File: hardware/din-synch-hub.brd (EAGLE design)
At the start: 140.7 x 20.2 mm, 47 parts, among them IC1 4050D, IC2 REG1117, IC3 4050D, IC4 PIC12F1822SO08, IC5 6N138, X1 DIN5PIN, X2 DIN5PIN, X3 DIN5PIN, X4 DIN5PIN, X5 DIN5PIN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

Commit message: fix bug
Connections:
- net N$4: now also X1.4; no longer X1.1
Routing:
- net N$4: track 10.3 -> 6.69 mm, vias 1 -> 0
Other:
- board text added: "six4pix.com/synchole"
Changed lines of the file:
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@@
 <text x="111.887" y="17.399" size="1.778" layer="21" font="vector">hotchk155</text>
 <text x="32.54375" y="15.24" size="3.81" layer="21" font="vector">Sync Hole</text>
+<text x="32.41675" y="7.4295" size="1.778" layer="21" font="vector">six4pix.com/synchole</text>
 </plain>
 <attributes>
@@
 </signal>
 <signal name="N$4">
-<contactref element="X1" pad="1"/>
 <contactref element="R18" pad="1"/>
-<wire x1="22.44725" y1="7.33675" x2="22.44725" y2="2.4765" width="0.3048" layer="16"/>
-<via x="23.495" y="1.42875" extent="1-16" drill="0.6"/>
-<wire x1="23.495" y1="3.302" x2="23.495" y2="4.445" width="0.3048" layer="1"/>
-<wire x1="23.495" y1="4.445" x2="22.86" y2="5.08" width="0.3048" layer="1"/>
-<wire x1="22.44725" y1="2.4765" x2="23.495" y2="1.42875" width="0.3048" layer="16"/>
-<wire x1="23.495" y1="1.42875" x2="23.495" y2="3.302" width="0.3048" layer="1"/>
+<contactref element="X1" pad="4"/>
+<wire x1="26.035" y1="3.302" x2="24.03475" y2="3.302" width="0.4064" layer="16"/>
+<wire x1="24.03475" y1="3.302" x2="22.44725" y2="4.8895" width="0.4064" layer="16"/>
+<wire x1="22.44725" y1="4.8895" x2="22.44725" y2="7.33675" width="0.4064" layer="16"/>
 </signal>
 <signal name="N$3">

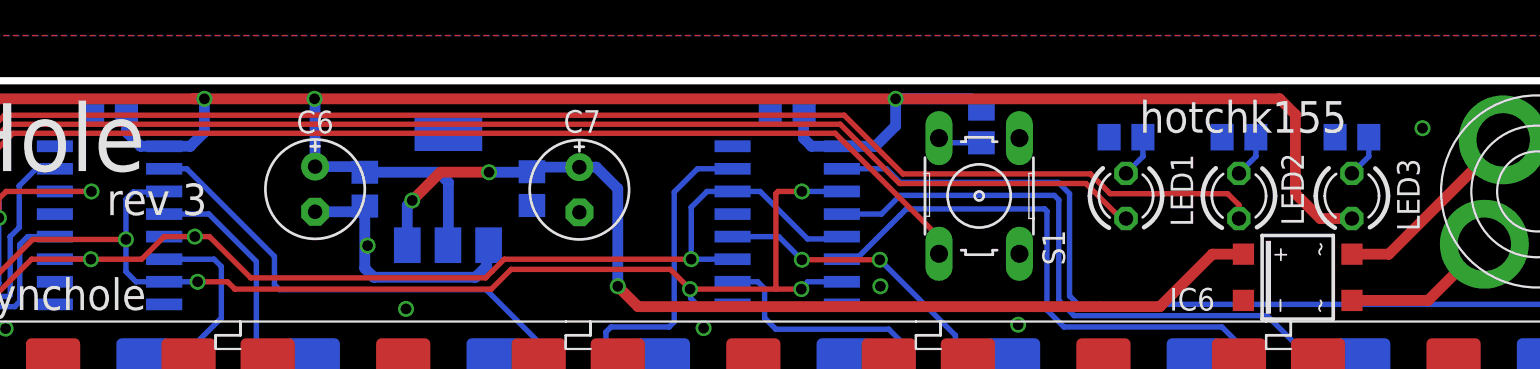
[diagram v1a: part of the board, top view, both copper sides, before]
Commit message: REV4
moved leds to match bsplit
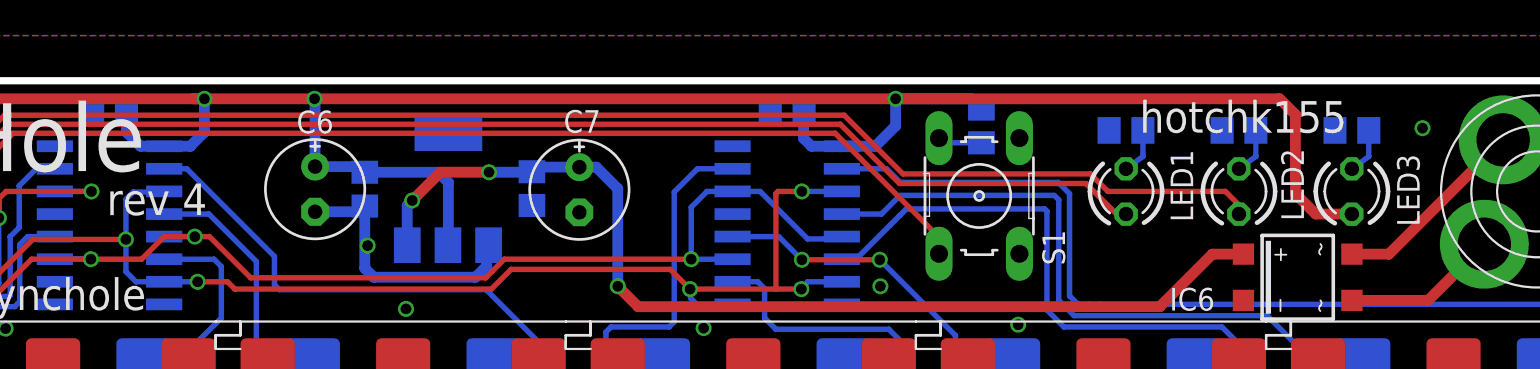
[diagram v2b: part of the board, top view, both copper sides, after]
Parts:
- moved R1 0.38 mm to (123.8, 17.5)
- moved R2 0.38 mm to (117.5, 17.5)
- moved R3 0.38 mm to (111.1, 17.5)
- moved LED1 0.25 mm to (111.1, 14.1)
- moved LED2 0.25 mm to (117.5, 14.1)
- moved LED3 0.25 mm to (123.8, 14.1)
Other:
- board text added: "rev 4"
- board text removed: "rev 3"
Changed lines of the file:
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@@
 <wire x1="139.192" y1="20.32" x2="140.843" y2="18.796" width="0.4064" layer="20" curve="-90"/>
 <wire x1="140.843" y1="18.796" x2="140.843" y2="1.27" width="0.4064" layer="20"/>
-<text x="53.81625" y="12.7635" size="1.778" layer="21" font="vector">rev 3</text>
+<text x="53.81625" y="12.7635" size="1.778" layer="21" font="vector">rev 4</text>
 <text x="111.887" y="17.399" size="1.778" layer="21" font="vector">hotchk155</text>
 <text x="32.54375" y="15.24" size="3.81" layer="21" font="vector">Sync Hole</text>
@@
 </class>
 </classes>
-<designrules name="ITEADstudio_DRC">
-<description language="de">&lt;b&gt;EAGLE Design Rules&lt;/b&gt;
+<designrules name="hackvana">
+<description language="de">&lt;b&gt;EAGLE Design Rules für Hackvana&lt;/b&gt;
 &lt;p&gt;
 Die Standard-Design-Rules sind so gewählt, dass sie für
@@
 Einstellungen hier und speichern die Design Rules unter
 einem neuen Namen ab.</description>
-<description language="en">&lt;b&gt;EAGLE Design Rules&lt;/b&gt;
+<description language="en">&lt;b&gt;EAGLE Design Rules for Hackvana&lt;/b&gt;
 &lt;p&gt;
 The default Design Rules have been set to cover
@@
 necessary adjustments and save your customized
 design rules under a new name.</description>
-<description language="zh">&lt;b&gt;Seeed Studio EAGLE Design Rules&lt;/b&gt;
+<description language="zh">&lt;b&gt;EAGLE Design Rules for Hackvana&lt;/b&gt;
 </description>
 <param name="layerSetup" value="(1*16)"/>
@@
 <param name="mtIsolate" value="1.5mm 0.15mm 0.2mm 0.15mm 0.2mm 0.15mm 0.2mm 0.15mm 0.2mm 0.15mm 0.2mm 0.15mm 0.2mm 0.15mm 0.2mm"/>
 <param name="mdWireWire" value="6mil"/>
-<param name="mdWirePad" value="6mil"/>
+<param name="mdWirePad" value="9mil"/>
 <param name="mdWireVia" value="6mil"/>
 <param name="mdPadPad" value="6mil"/>
@@
 <param name="mdViaViaSameLayer" value="8mil"/>
 <param name="mnLayersViaInSmd" value="2"/>
-<param name="mdCopperDimension" value="10mil"/>
-<param name="mdDrill" value="10mil"/>
+<param name="mdCopperDimension" value="6mil"/>
+<param name="mdDrill" value="6mil"/>
 <param name="mdSmdStop" value="0mil"/>
 <param name="msWidth" value="6mil"/>
-<param name="msDrill" value="12mil"/>
-<param name="msMicroVia" value="12mil"/>
+<param name="msDrill" value="0.3mm"/>
+<param name="msMicroVia" value="0.25mm"/>
 <param name="msBlindViaRatio" value="0.5"/>
 <param name="rvPadTop" value="0.25"/>
@@
 <attribute name="VALUE" x="97.79" y="16.891" size="1.27" layer="27" ratio="10" rot="R270"/>
 </element>
-<element name="LED1" library="led" package="LED3MM" value="" x="111.125" y="13.843" smashed="yes" rot="R90">
-<attribute name="NAME" x="113.63325" y="16.1925" size="1.27" layer="25" ratio="10" rot="R270"/>
-<attribute name="VALUE" x="112.776" y="15.748" size="1.27" layer="27" ratio="10" rot="R90"/>
-</element>
-<element name="R3" library="rcl" package="R0805" value="" x="111.125" y="17.145" smashed="yes" rot="MR180">
-<attribute name="NAME" x="109.7915" y="19.71675" size="1.27" layer="26" rot="MR180"/>
-<attribute name="VALUE" x="110.49" y="19.685" size="1.27" layer="28" rot="MR180"/>
-</element>
-<element name="LED2" library="led" package="LED3MM" value="" x="117.475" y="13.843" smashed="yes" rot="R90">
-<attribute name="NAME" x="119.85625" y="16.256" size="1.27" layer="25" ratio="10" rot="R270"/>
-<attribute name="VALUE" x="119.126" y="15.748" size="1.27" layer="27" ratio="10" rot="R90"/>
-</element>
-<element name="R2" library="rcl" package="R0805" value="" x="117.475" y="17.145" smashed="yes" rot="MR180">
-<attribute name="NAME" x="116.459" y="19.685" size="1.27" layer="26" rot="MR180"/>
-<attribute name="VALUE" x="116.84" y="19.685" size="1.27" layer="28" rot="MR180"/>
+<element name="LED1" library="led" package="LED3MM" value="" x="111.125" y="14.097" smashed="yes" rot="R90">
+<attribute name="NAME" x="113.63325" y="16.4465" size="1.27" layer="25" ratio="10" rot="R270"/>
+<attribute name="VALUE" x="112.776" y="16.002" size="1.27" layer="27" ratio="10" rot="R90"/>
+</element>
+<element name="R3" library="rcl" package="R0805" value="" x="111.125" y="17.526" smashed="yes" rot="MR180">
+<attribute name="NAME" x="109.9185" y="19.8755" size="1.27" layer="26" rot="MR180"/>
+<attribute name="VALUE" x="110.49" y="20.066" size="1.27" layer="28" rot="MR180"/>
+</element>
+<element name="LED2" library="led" package="LED3MM" value="" x="117.475" y="14.097" smashed="yes" rot="R90">
+<attribute name="NAME" x="119.85625" y="16.51" size="1.27" layer="25" ratio="10" rot="R270"/>
+<attribute name="VALUE" x="119.126" y="16.002" size="1.27" layer="27" ratio="10" rot="R90"/>
+</element>
+<element name="R2" library="rcl" package="R0805" value="" x="117.475" y="17.526" smashed="yes" rot="MR180">
+<attribute name="NAME" x="116.332" y="19.8755" size="1.27" layer="26" rot="MR180"/>
+<attribute name="VALUE" x="116.84" y="20.066" size="1.27" layer="28" rot="MR180"/>
 </element>
 <element name="IC2" library="burr-brown" package="SOT223" value="REG1117" x="73.025" y="14.224" smashed="yes" rot="MR0">
@@
 <attribute name="VALUE" x="62.992" y="11.557" size="1.27" layer="27" ratio="10" rot="R270"/>
 </element>
-<element name="R1" library="rcl" package="R0805" value="" x="123.825" y="17.145" smashed="yes" rot="MR180">
-<attribute name="NAME" x="123.09475" y="19.6215" size="1.27" layer="26" rot="MR180"/>
-<attribute name="VALUE" x="123.19" y="19.685" size="1.27" layer="28" rot="MR180"/>
-</element>
-<element name="LED3" library="led" package="LED3MM" value="" x="123.825" y="13.843" smashed="yes" rot="R90">
-<attribute name="NAME" x="126.365" y="15.9385" size="1.27" layer="25" ratio="10" rot="R270"/>
-<attribute name="VALUE" x="125.476" y="15.748" size="1.27" layer="27" ratio="10" rot="R90"/>
+<element name="R1" library="rcl" package="R0805" value="" x="123.825" y="17.526" smashed="yes" rot="MR180">
+<attribute name="NAME" x="122.4915" y="19.84375" size="1.27" layer="26" rot="MR180"/>
+<attribute name="VALUE" x="123.19" y="20.066" size="1.27" layer="28" rot="MR180"/>
+</element>
+<element name="LED3" library="led" package="LED3MM" value="" x="123.825" y="14.097" smashed="yes" rot="R90">
+<attribute name="NAME" x="126.365" y="16.1925" size="1.27" layer="25" ratio="10" rot="R270"/>
+<attribute name="VALUE" x="125.476" y="16.002" size="1.27" layer="27" ratio="10" rot="R90"/>
 </element>
 <element name="U$1" library="jason_eagle6" package="PWR_SOCKET_2_1MM" value="PWR_SOCKET_2_1MM" x="134.239" y="14.097" smashed="yes" rot="R135"/>
@@
 <wire x1="119.761" y1="19.304" x2="120.65" y2="18.415" width="0.6096" layer="1"/>
 <wire x1="120.65" y1="18.415" x2="120.65" y2="13.97" width="0.6096" layer="1"/>
-<wire x1="120.65" y1="13.97" x2="122.047" y2="12.573" width="0.6096" layer="1"/>
-<wire x1="122.047" y1="12.573" x2="123.825" y2="12.573" width="0.6096" layer="1"/>
+<wire x1="120.65" y1="13.97" x2="121.793" y2="12.827" width="0.6096" layer="1"/>
+<wire x1="121.793" y1="12.827" x2="123.825" y2="12.827" width="0.6096" layer="1"/>
 </signal>
 <signal name="N$14">
@@
 <contactref element="IC4" pad="3"/>
 <contactref element="LED1" pad="A"/>
-<wire x1="111.125" y1="12.573" x2="110.83925" y2="12.573" width="0.3048" layer="1"/>
+<wire x1="111.125" y1="12.827" x2="110.83925" y2="12.573" width="0.3048" layer="1"/>
 <wire x1="110.83925" y1="12.573" x2="108.87075" y2="14.5415" width="0.3048" layer="1"/>
 <wire x1="108.87075" y1="14.5415" x2="98.39325" y2="14.5415" width="0.3048" layer="1"/>
@@
 <contactref element="IC4" pad="5"/>
 <contactref element="LED2" pad="A"/>
-<wire x1="117.475" y1="12.573" x2="117.475" y2="13.335" width="0.3048" layer="1"/>
-<wire x1="117.475" y1="13.335" x2="116.84" y2="13.97" width="0.3048" layer="1"/>
-<wire x1="116.84" y1="13.97" x2="110.236" y2="13.97" width="0.3048" layer="1"/>
-<wire x1="110.236" y1="13.97" x2="109.12475" y2="15.08125" width="0.3048" layer="1"/>
+<wire x1="117.475" y1="12.827" x2="117.475" y2="13.335" width="0.3048" layer="1"/>
+<wire x1="117.475" y1="13.335" x2="116.713" y2="14.097" width="0.3048" layer="1"/>
+<wire x1="116.713" y1="14.097" x2="110.109" y2="14.097" width="0.3048" layer="1"/>
+<wire x1="110.109" y1="14.097" x2="109.12475" y2="15.08125" width="0.3048" layer="1"/>
 <wire x1="109.12475" y1="15.08125" x2="98.58375" y2="15.08125" width="0.3048" layer="1"/>
 <wire x1="38.5318" y1="11.303" x2="38.5318" y2="10.1727" width="0.3048" layer="16"/>
@@
 <contactref element="R1" pad="2"/>
 <contactref element="LED3" pad="K"/>
-<wire x1="124.775" y1="17.145" x2="124.775" y2="16.063" width="0.3048" layer="16"/>
-<wire x1="124.775" y1="16.063" x2="123.825" y2="15.113" width="0.3048" layer="16"/>
+<wire x1="124.775" y1="17.526" x2="124.775" y2="16.063" width="0.3048" layer="16"/>
+<wire x1="124.775" y1="16.063" x2="123.825" y2="15.367" width="0.3048" layer="16"/>
 </signal>
 <signal name="N$31">
 <contactref element="R2" pad="2"/>
 <contactref element="LED2" pad="K"/>
-<wire x1="118.425" y1="17.145" x2="118.425" y2="16.063" width="0.3048" layer="16"/>
-<wire x1="118.425" y1="16.063" x2="117.475" y2="15.113" width="0.3048" layer="16"/>
+<wire x1="118.425" y1="17.526" x2="118.425" y2="16.063" width="0.3048" layer="16"/>
+<wire x1="118.425" y1="16.063" x2="117.475" y2="15.367" width="0.3048" layer="16"/>
 </signal>
 <signal name="N$33">
 <contactref element="R3" pad="2"/>
 <contactref element="LED1" pad="K"/>
-<wire x1="112.075" y1="17.145" x2="112.075" y2="16.063" width="0.3048" layer="16"/>
-<wire x1="112.075" y1="16.063" x2="111.125" y2="15.113" width="0.3048" layer="16"/>
+<wire x1="112.075" y1="17.526" x2="112.075" y2="16.063" width="0.3048" layer="16"/>
+<wire x1="112.075" y1="16.063" x2="111.125" y2="15.367" width="0.3048" layer="16"/>
 </signal>
 <signal name="MIDI">

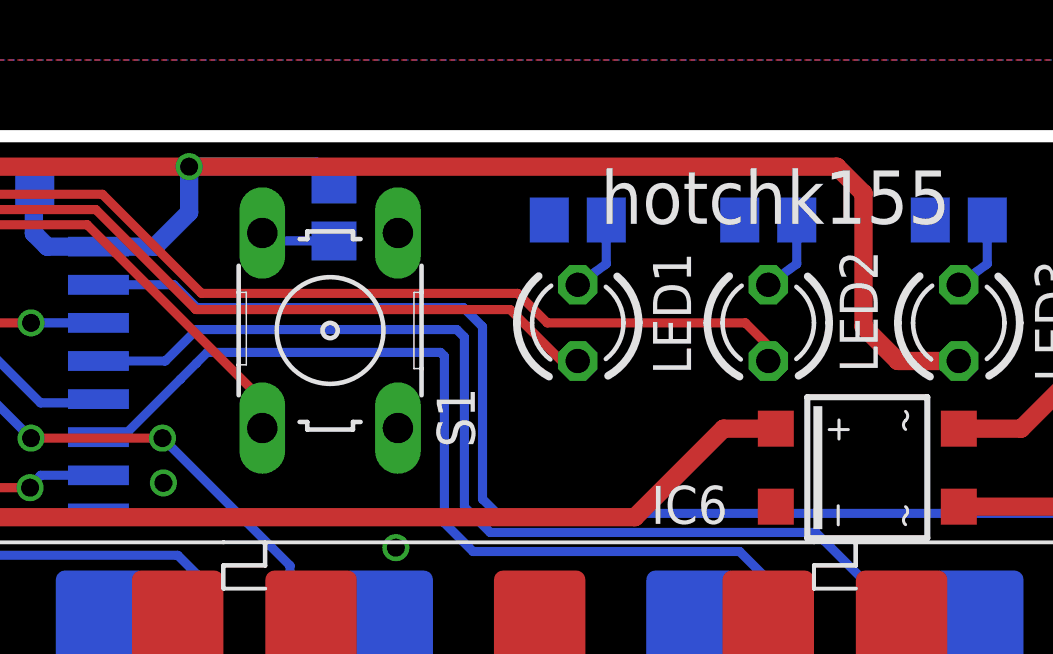
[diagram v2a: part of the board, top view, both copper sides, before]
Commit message: move switch (rev4 pcb)
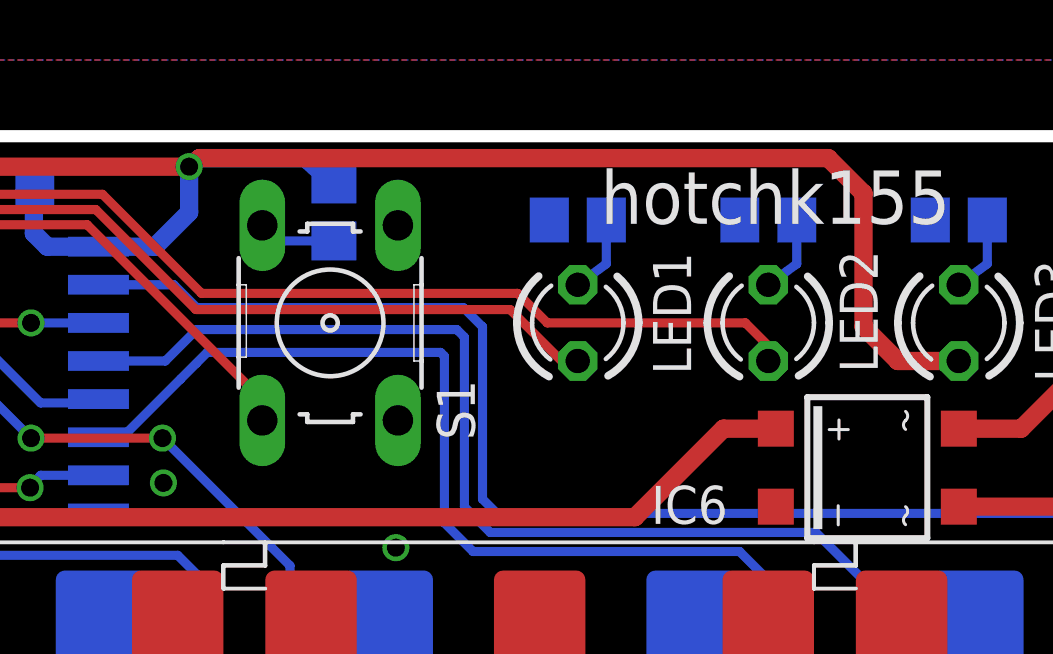
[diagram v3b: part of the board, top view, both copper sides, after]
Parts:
- moved S1 0.25 mm to (102.9, 14.1)
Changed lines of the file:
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@@
 <attribute name="VALUE" x="100.457" y="17.145" size="1.27" layer="28" rot="MR90"/>
 </element>
-<element name="S1" library="switch-omron" package="B3F-10XX" value="" x="102.87" y="13.843" smashed="yes" rot="R270">
-<attribute name="OC_NEWARK" value="36M3542" x="53.34" y="-48.387" size="1.778" layer="27" rot="R270" display="off"/>
-<attribute name="MPN" value="B3F-1000" x="53.34" y="-48.387" size="1.778" layer="27" rot="R270" display="off"/>
-<attribute name="MF" value="" x="53.34" y="-48.387" size="1.778" layer="27" rot="R270" display="off"/>
-<attribute name="OC_FARNELL" value="176432" x="53.34" y="-48.387" size="1.778" layer="27" rot="R270" display="off"/>
-<attribute name="NAME" x="106.426" y="11.938" size="1.27" layer="25" ratio="10" rot="R270"/>
-<attribute name="VALUE" x="97.79" y="16.891" size="1.27" layer="27" ratio="10" rot="R270"/>
+<element name="S1" library="switch-omron" package="B3F-10XX" value="" x="102.87" y="14.097" smashed="yes" rot="R270">
+<attribute name="OC_NEWARK" value="36M3542" x="53.34" y="-48.133" size="1.778" layer="27" rot="R270" display="off"/>
+<attribute name="MPN" value="B3F-1000" x="53.34" y="-48.133" size="1.778" layer="27" rot="R270" display="off"/>
+<attribute name="MF" value="" x="53.34" y="-48.133" size="1.778" layer="27" rot="R270" display="off"/>
+<attribute name="OC_FARNELL" value="176432" x="53.34" y="-48.133" size="1.778" layer="27" rot="R270" display="off"/>
+<attribute name="NAME" x="106.426" y="12.192" size="1.27" layer="25" ratio="10" rot="R270"/>
+<attribute name="VALUE" x="97.79" y="17.145" size="1.27" layer="27" ratio="10" rot="R270"/>
 </element>
 <element name="LED1" library="led" package="LED3MM" value="" x="111.125" y="14.097" smashed="yes" rot="R90">
@@
 <wire x1="42.51325" y1="19.304" x2="59.309" y2="19.304" width="0.6096" layer="1"/>
 <wire x1="65.50025" y1="19.304" x2="98.171" y2="19.304" width="0.6096" layer="1"/>
-<wire x1="98.171" y1="19.304" x2="102.423" y2="19.304" width="0.6096" layer="16"/>
-<wire x1="102.423" y1="19.304" x2="102.997" y2="18.73" width="0.6096" layer="16"/>
+<wire x1="102.042" y1="19.58975" x2="102.997" y2="18.73" width="0.6096" layer="16"/>
 <wire x1="43.7642" y1="15.113" x2="43.7642" y2="16.4973" width="0.6096" layer="16"/>
 <wire x1="43.7642" y1="16.4973" x2="42.9895" y2="17.272" width="0.6096" layer="16"/>
@@
 <wire x1="30.607" y1="15.14475" x2="33.24225" y2="15.14475" width="0.6096" layer="16"/>
 <wire x1="33.24225" y1="15.14475" x2="33.274" y2="15.113" width="0.6096" layer="16"/>
-<wire x1="98.171" y1="19.304" x2="119.761" y2="19.304" width="0.6096" layer="1"/>
-<wire x1="119.761" y1="19.304" x2="120.65" y2="18.415" width="0.6096" layer="1"/>
+<wire x1="119.47525" y1="19.58975" x2="120.65" y2="18.415" width="0.6096" layer="1"/>
 <wire x1="120.65" y1="18.415" x2="120.65" y2="13.97" width="0.6096" layer="1"/>
 <wire x1="120.65" y1="13.97" x2="121.793" y2="12.827" width="0.6096" layer="1"/>
 <wire x1="121.793" y1="12.827" x2="123.825" y2="12.827" width="0.6096" layer="1"/>
+<wire x1="98.171" y1="19.304" x2="98.52025" y2="19.58975" width="0.6096" layer="1"/>
+<wire x1="98.52025" y1="19.58975" x2="119.47525" y2="19.58975" width="0.6096" layer="1"/>
+<wire x1="98.171" y1="19.304" x2="98.52025" y2="19.58975" width="0.6096" layer="16"/>
+<wire x1="98.52025" y1="19.58975" x2="102.042" y2="19.58975" width="0.6096" layer="16"/>
 </signal>
 <signal name="N$14">
@@
 <contactref element="R4" pad="1"/>
 <wire x1="102.997" y1="16.83" x2="100.8736" y2="16.83" width="0.3048" layer="16"/>
-<wire x1="100.8736" y1="16.83" x2="100.6094" y2="17.0942" width="0.3048" layer="16"/>
-<wire x1="100.6094" y1="10.5918" x2="100.6094" y2="11.5316" width="0.3048" layer="1"/>
+<wire x1="100.8736" y1="16.83" x2="100.6094" y2="17.3482" width="0.3048" layer="16"/>
+<wire x1="100.6094" y1="10.8458" x2="100.6094" y2="11.5316" width="0.3048" layer="1"/>
 <via x="36.703" y="17.272" extent="1-16" drill="0.6"/>
 <wire x1="37.846" y1="17.0815" x2="37.846" y2="11.6205" width="0.3048" layer="1"/>
